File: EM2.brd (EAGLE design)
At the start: 101.6 x 53.3 mm, 120 parts, among them IC1 EUP3476SO08T, IC2 APX811-44UG-7, IC3 ATMEGA16U2-MU, IC4 MCP24AA025E48, IC6 W5100SQFP80, IC9 ATMEGA2560-16AU, J1 DC_2_1MM, P1 USB-6PSMT, P3 ICSP:USB, P4 microSD, Q2 2N7002, Q3 2N7002, U1 HY931147C-RJ45, X1 16MHz, X2 25MHz, X3 16MHz

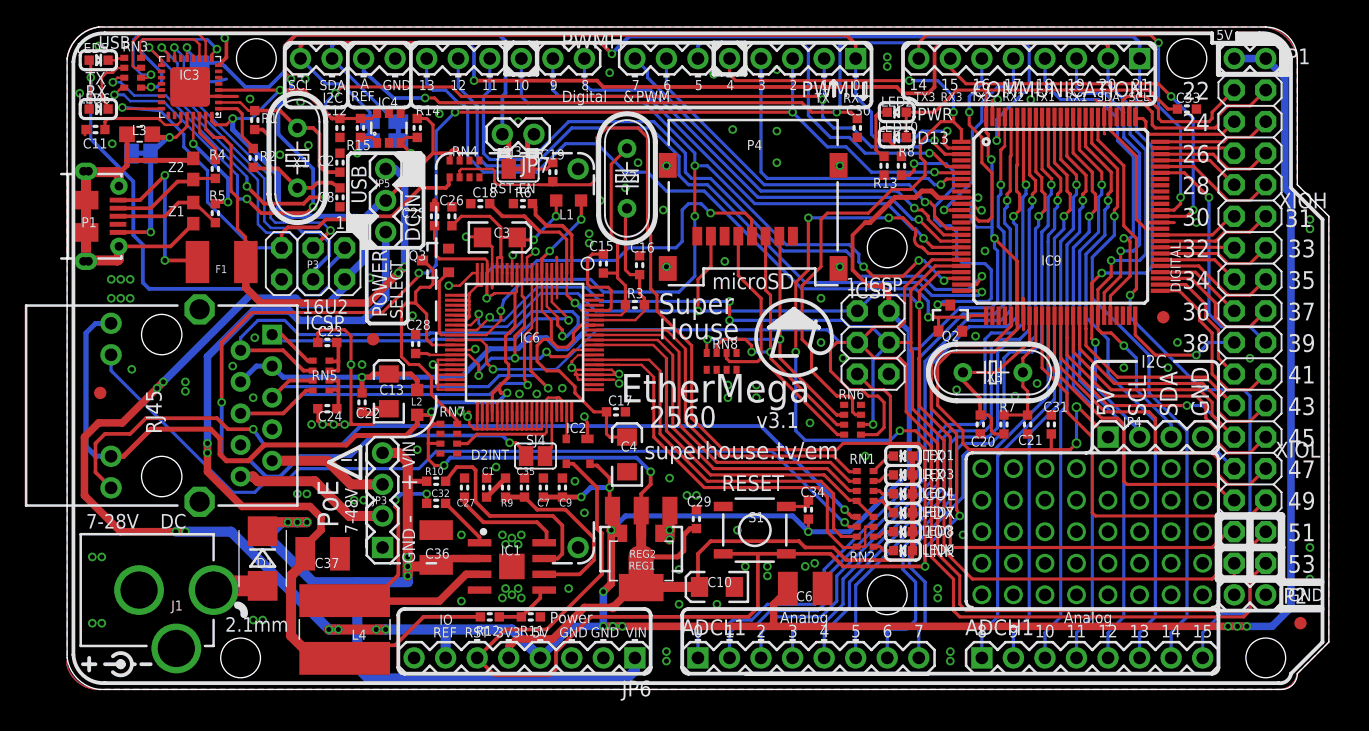
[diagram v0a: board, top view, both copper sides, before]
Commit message: Major rework using W5500 ethernet chip
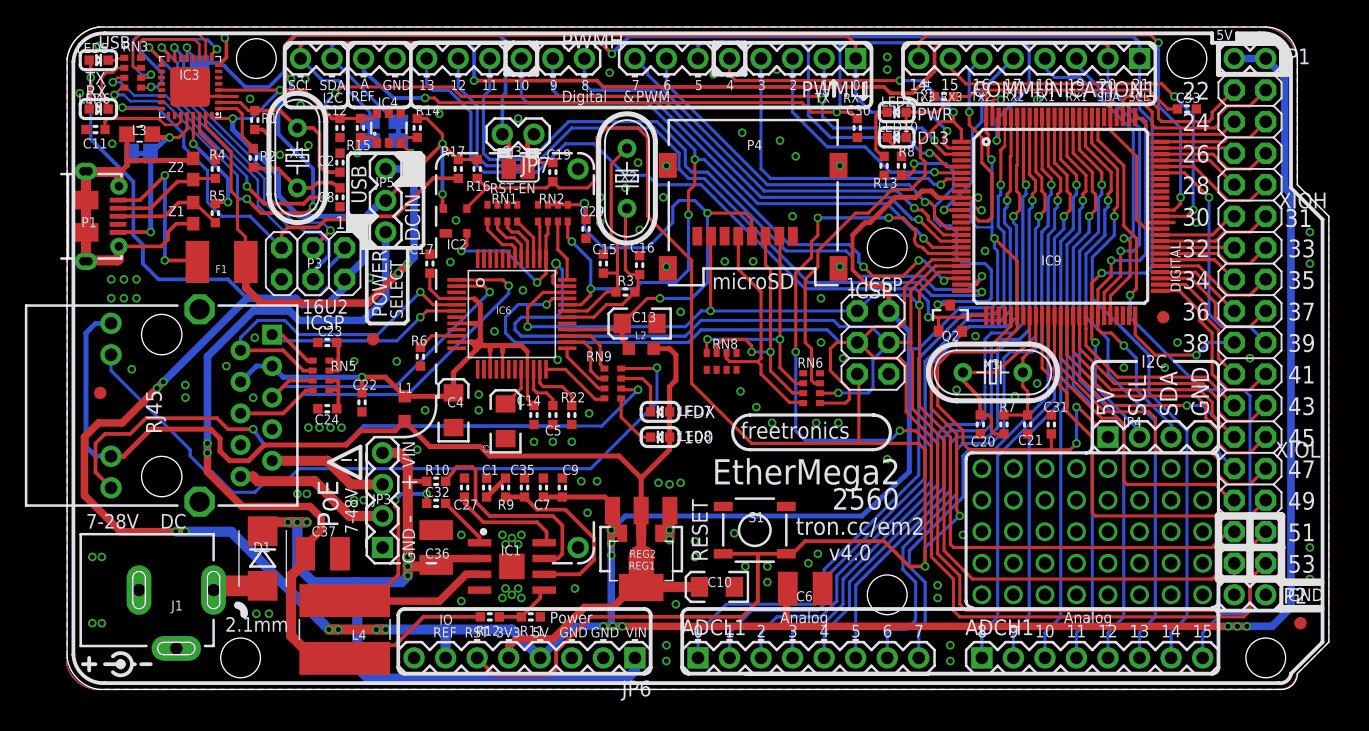
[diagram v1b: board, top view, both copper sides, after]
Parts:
- removed C18: 10nF, freetronics-marc:0603
- removed C25, C26, C28: 100nF, freetronics-marc:0603
- removed LED1, LED3, LED9: YELLOW, freetronics-jon:LED-0603
- removed LED4: RED, freetronics-jon:LED-0603
- removed Q3: 2N7002, freetronics:SOT23-3
- removed RN4: 10K, freetronics-master-v1:CAY16
- removed RN7: 1K, freetronics-master-v1:CAY16
- removed SJ4: D2_INT, jumper:SJ
- added C14: 100nF, freetronics-jon:0603
- added C5: 10nF, freetronics-jon:0603
- added R16, R17: 10K 0603, freetronics-marc:0603
- added R22: 10K, freetronics-marc:0603
- added RN9: 1K, freetronics-master-v1.1:CAY16
- C17: device freetronics-marc:0603 -> freetronics-jon:0603
- C3: value 10uF 6.3V A TANT -> 4.7uF 6.3V A TANT
- IC6: value W5100SQFP80 -> W5500; device freetronics-marc:SQFP80 -> W5500:W5500
- J1: device freetronics:POWER_JACK_PTH -> freetronics-jon:POWER_JACK_PTH_SLOTS
- L1, L2: value 1uH 250mA 0805 -> Bourns MH2029-300Y 30R 3A 0805
- LED8: value GREEN -> YELLOW
- RN1, RN2: value 1K -> 10K; device freetronics-master-v1:CAY16 -> freetronics-master-v1.1:CAY16
- SJ1, SJ3: device jumper:SJ -> freetronics-jon:SJC
- moved RN1 36.6 mm to (35.1, 38.4), turned to 0 degrees
- moved RN2 35.9 mm to (39.1, 38.4), turned to 0 degrees
- moved C34 35.0 mm to (70.6, 47.8), turned to 180 degrees
- moved C29 25.0 mm to (41.8, 37.1), turned to 270 degrees
- moved L1 21.3 mm to (27.2, 22.6), turned to 90 degrees
- moved LED7 21.2 mm to (47.8, 22.4)
- moved IC2 21.0 mm to (31.2, 37.7), turned to 0 degrees
- moved LED8 21.0 mm to (47.8, 20.3)
- moved C13 20.9 mm to (46.1, 29.5), turned to 180 degrees
- moved C17 19.2 mm to (29.2, 34.3), turned to 90 degrees
- moved L2 18.5 mm to (46.2, 27.4), turned to 180 degrees
- moved R6 14.8 mm to (28.4, 26.8), turned to 90 degrees
- moved C3 14.8 mm to (35.3, 21.6), turned to 90 degrees
- moved C4 14.4 mm to (31.1, 22.5)
- moved RN6 4.17 mm to (59.9, 24.3)
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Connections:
- removed net 1V8A: C17.1, C4.A, IC6.7, IC6.74, L1.2
- removed net 1V8_OUT: C26.1, C28.1, C3.A, IC6.11, IC6.15, IC6.16, IC6.33, IC6.69, L1.1
- removed net COLLED: IC6.71, RN1.3
- removed net D10: IC6.29, IC9.23, PWMH.3, Q3.1
- removed net N$27: IC6.55, IC6.57, IC6.58, RN7.2
- removed net N$322: IC6.1, R6.2
- removed net N$328: LED4.C, RN1.6
- removed net N$330: LED1.C, RN1.8
- removed net N$332: RN2.2, U1.P$12
- removed net N$67: RN2.1, U1.P$14
- removed net SEN: IC6.31, Q3.3, RN7.4
- removed net WRXLED: IC6.72, RN1.2
- removed net WTXLED: IC6.73, RN1.1
- new net 3.3V: C10.A, JP6.5, L1.1, L2.1, LED7.A, LED8.A, REG1.2, REG1.4, REG2.2, REG2.4, U1.P$11, U1.P$13
- new net ACTLED: IC6.27, RN9.1
- new net D10_SS: IC6.32, IC9.23, PWMH.3, RN2.4
- new net EXRES1: IC6.10, R6.2
- new net INT: IC6.36, RN2.3
- new net N$63: IC6.40, RN1.3
- new net N$73: IC6.41, RN1.2
- new net N$76: IC6.42, RN1.1
- new net N$78: IC6.23, R22.2
- new net N$79: IC6.38, RN2.1
- new net N$80: C5.1, IC6.22
- new net N$81: C3.A, IC6.20
- new net PMODE0: IC6.45
- new net PMODE1: IC6.44
- new net PMODE2: IC6.43
- net 3V3A: now also C14.1, C17.1, C4.A, IC6.11, IC6.15, IC6.17, IC6.21, IC6.4, IC6.8, L1.2; no longer C13.A, C18.1, IC6.2, L2.2
- net 3V3D: now also C13.A, IC6.28, L2.2, RN2.5, RN2.6, RN2.7; no longer C10.A, C25.1, IC6.12, IC6.18, IC6.44, JP6.5, L2.1, LED1.A, LED3.A, LED4.A, LED7.A, LED8.A, LED9.A, REG1.2, REG1.4, REG2.2, REG2.4, RN7.5, RN7.7, U1.P$11, U1.P$13
- net 5V: now also R16.2, R17.2; no longer RN4.7, RN4.8
- net D2: no longer SJ4.1
- net D50_MISO: now also IC6.34; no longer IC6.27
- net D51_MOSI: now also IC6.35; no longer IC6.28
- net D52_SCK: now also IC6.33; no longer IC6.30
- net FDXLED: now also IC6.26, RN9.2; no longer IC6.70, RN1.4, RN2.8
- net GND: now also C14.2, C5.2, IC6.16, IC6.29, IC6.3, IC6.9, R22.1, RN1.5, RN1.6, RN1.7, RN1.8, RN2.8; no longer C18.2, C25.2, C26.2, C28.2, IC6.10, IC6.13, IC6.17, IC6.20, IC6.21, IC6.22, IC6.23, IC6.24, IC6.25, IC6.26, IC6.32, IC6.34, IC6.35, IC6.36, IC6.37, IC6.38, IC6.39, IC6.4, IC6.40, IC6.41, IC6.42, IC6.43, IC6.45, IC6.46, IC6.47, IC6.49, IC6.50, IC6.51, IC6.52, IC6.53, IC6.54, IC6.63, IC6.64, IC6.65, IC6.68, IC6.77, Q3.2
- net LINKLED: now also IC6.25, RN9.3; no longer IC6.66, RN2.4, RN2.7
- net N$26: now also RN9.5; no longer RN2.6
- net N$28: now also RN9.6, U1.P$14; no longer LED9.C, RN2.5
- net N$327: now also RN9.7; no longer RN1.5
- net N$329: now also RN9.8, U1.P$12; no longer LED3.C, RN1.7
- net N$62: now also IC6.39, RN1.4; no longer IC6.56, SJ4.2
- net RESET: now also R16.1; no longer RN4.2
- net RESET2: now also R17.1; no longer RN4.1
- net RXIN: now also IC6.5; no longer IC6.6
- net RXIP: now also IC6.6; no longer IC6.5
- net SPDLED: now also IC6.24, RN9.4; no longer IC6.67, RN2.3
- net TXON: now also IC6.1; no longer IC6.9
- net TXOP: now also IC6.2; no longer IC6.8
- net WIZRST: now also IC6.37, RN2.2; no longer IC6.59
- net XTLN: now also C15.1, IC6.31, R3.1, X2.1; no longer C16.1, IC6.75, R3.2, X2.2
- net XTLP: now also C16.1, IC6.30, R3.2, X2.2; no longer C15.1, IC6.76, R3.1, X2.1
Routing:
- net 3V3D: track 194.2 -> 45.4 mm, vias 6 -> 3
- net GND: track 138.7 -> 13.7 mm
- net 3.3V: track 0.00 -> 103.4 mm
- net D2: track 117.0 -> 19.9 mm, vias 6 -> 1
- net D10: track 85.0 -> 0.00 mm, vias 6 -> 0
- net D10_SS: track 0.00 -> 73.1 mm, vias 0 -> 7
- net N$67: track 70.9 -> 0.00 mm, vias 2 -> 0
- net N$332: track 69.3 -> 0.00 mm, vias 1 -> 0
- net N$329: track 1.81 -> 58.3 mm, vias 0 -> 1
- net N$28: track 1.75 -> 52.9 mm, vias 0 -> 2
- net 1V8_OUT: track 44.2 -> 0.00 mm, vias 5 -> 0
- net 1V8A: track 31.5 -> 0.00 mm, vias 2 -> 0
- net LINKLED: track 34.8 -> 4.74 mm
- net COLLED: track 29.6 -> 0.00 mm
- net WRXLED: track 29.5 -> 0.00 mm
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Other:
- board text added: "EtherMega2"
- board text added: "freetronics"
- board text added: "tron.cc/em2"
- board text added: "v4.0"
- board text added: "www.freetronics.com.au/em2"
- board text removed: "2560 R3"
- board text removed: "COL"
- board text removed: "D2INT"
- board text removed: "House"
- board text removed: "LNK"
- board text removed: "Super"
- board text removed: "SuperHouse"
- board text removed: "superhouse.tv/em"
- board text removed: "v3.1"
- board text removed: "www.superhouse.tv/em"
